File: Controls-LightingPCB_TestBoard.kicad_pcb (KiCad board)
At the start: 2 copper layers, 92 x 84 mm, 52 parts, among them J1 +12V, J10 REGEN SW, J11 CRUZ ST IND, J12 CRUZ EN IND, J13 REGEN IND, J14 NEU IND, J15 FOR IND, J16 REV IND, J17 EXT RBLINK, J18 EXT LBLINK, J19 INT RBLINK, J2 GND, J20 INT LBLINK, J21 EXT HDLT, J22 EXT BRAKE, J3 POWER MINION, J4 POWER LEADER, J5 TURN SIG SW, J6 CRUISE EN, J7 CRUISE SET, J8 HZD SW, J9 F/R SW, SW2 SW_SPST, SW3 SW_SPST, SW4 SW_SPST, SW6 SW_SPST, U1 SP3T, U2 SP3T

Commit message: update QUAC
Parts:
- added H1: MountingHole, MountingHole:MountingHole_3mm, F.Cu at (103.5, 62.0)
- added H2: MountingHole, MountingHole:MountingHole_3mm, F.Cu at (187.6, 62.2)
- added H3: MountingHole, MountingHole:MountingHole_3mm, F.Cu at (103.6, 142.2)
- added H4: MountingHole, MountingHole:MountingHole_3mm, F.Cu at (187.6, 142.2)
- added LOGO1: Logo_Placeholder, UTSVT_Special:UTSVT_Logo_Symbol, F.Cu at (174.6, 119.2)
- added LOGO2: Logo_Placeholder, UTSVT_Special:Hallock_Image_Tiny, B.Cu at (134.6, 66.2)
- J10, J15: footprint Connector_Molex:Molex_Micro-Fit_3.0_43650-0200_1x02_P3.00mm_Horizontal -> Connector_Molex:Molex_Micro-Fit_3.0_43650-0215_1x02_P3.00mm_Vertical
- moved D11 54.7 mm to (134.7, 84.3)
- moved D12 54.7 mm to (134.7, 97.0)
- moved D7 54.7 mm to (134.7, 122.4)
- moved D8 54.7 mm to (134.7, 109.7)
- moved J1 54.7 mm to (125.3, 68.6)
- moved J9 54.7 mm to (186.7, 75.6)
- moved R11 54.7 mm to (134.7, 80.0)
- moved R12 54.7 mm to (134.8, 92.2)
- moved R4 54.7 mm to (152.2, 105.0)
- moved R5 54.7 mm to (152.2, 92.2)
- moved R6 54.7 mm to (152.2, 116.9)
- moved R7 54.7 mm to (134.8, 116.9)
- moved R8 54.7 mm to (134.8, 105.0)
- moved SW2 54.7 mm to (164.3, 117.7)
- moved SW3 54.7 mm to (164.3, 104.5)
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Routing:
- net Net-(J1-Pad1): track 80.8 -> 64.4 mm
- net Net-(J2-Pad1): track 41.0 -> 29.9 mm
- net Net-(J10-Pad1): track 22.7 -> 24.6 mm
- net Net-(D5-Pad1): track 70.2 -> 71.4 mm
- net Net-(J15-Pad1): track 84.8 -> 85.3 mm
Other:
- board size 92 x 84 mm -> 92 x 88 mm
- board text added: "VER 0.1"

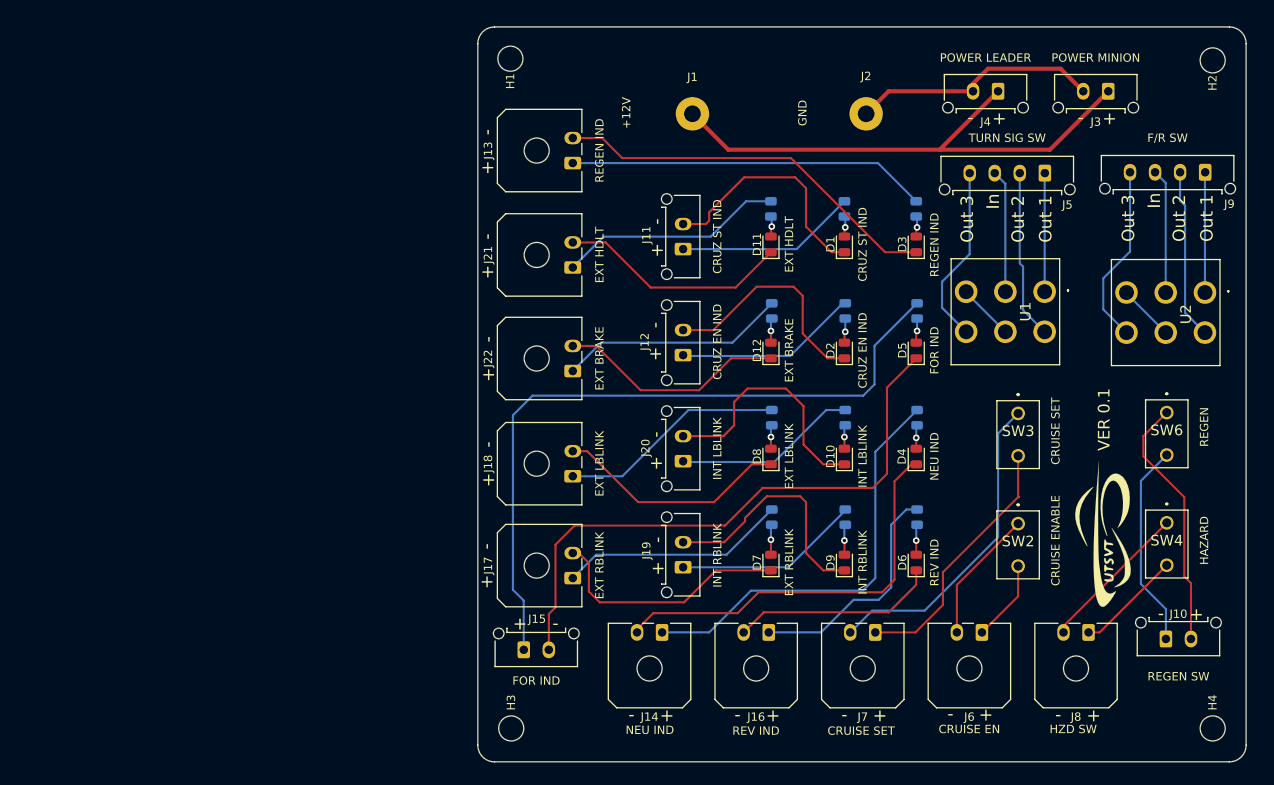
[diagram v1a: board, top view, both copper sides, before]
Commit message: checklist wrap up, and ground plane added
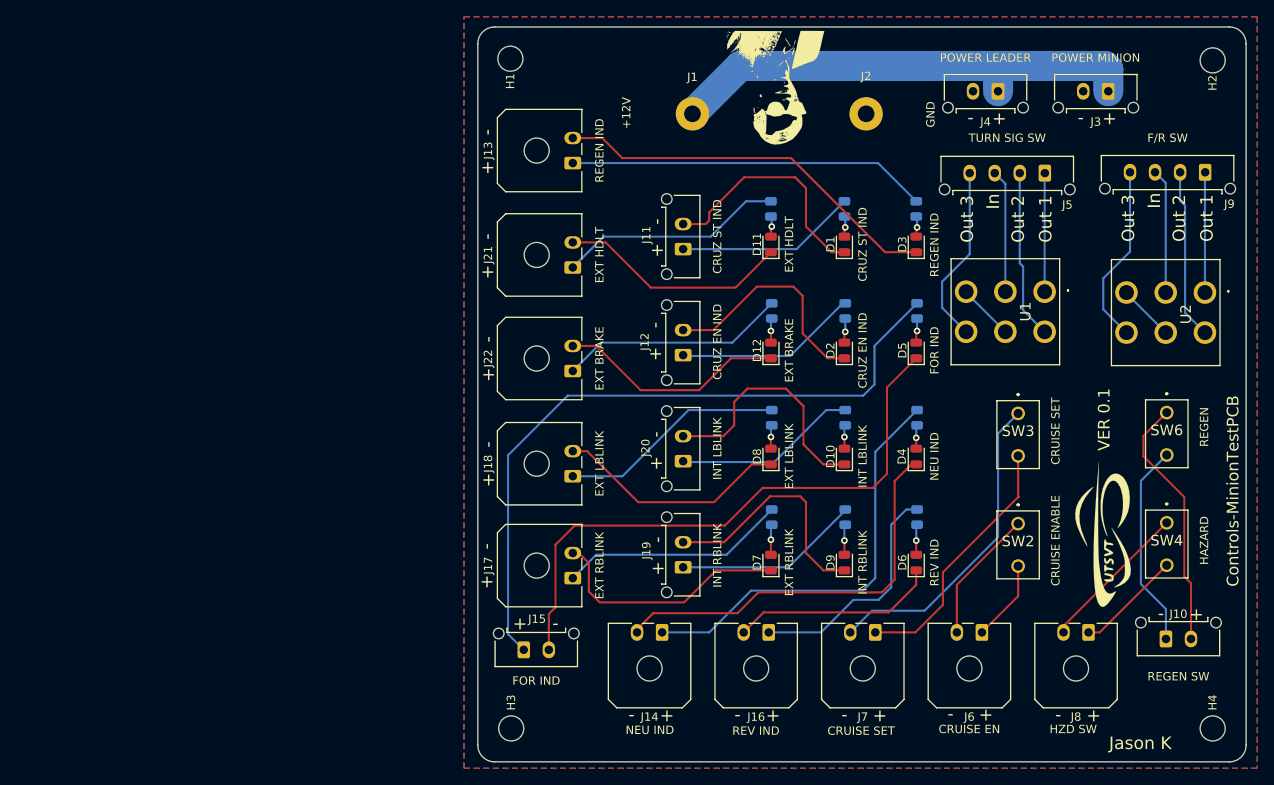
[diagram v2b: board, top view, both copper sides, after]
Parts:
- LOGO2: moved to F.Cu
- moved LOGO2 1.26 mm to (135.7, 65.7), turned to 180 degrees
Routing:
- net Net-(J2-Pad1): track 29.9 -> 0.00 mm
- net Net-(J1-Pad1): track 64.4 -> 58.0 mm
- net Net-(J15-Pad1): track 85.3 -> 83.3 mm
- added copper zone on B.Cu, net Net-(J2-Pad1)
- added copper zone on F.Cu, net Net-(J2-Pad1)
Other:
- board text added: "Controls-MinionTestPCB"
- board text added: "Jason K"

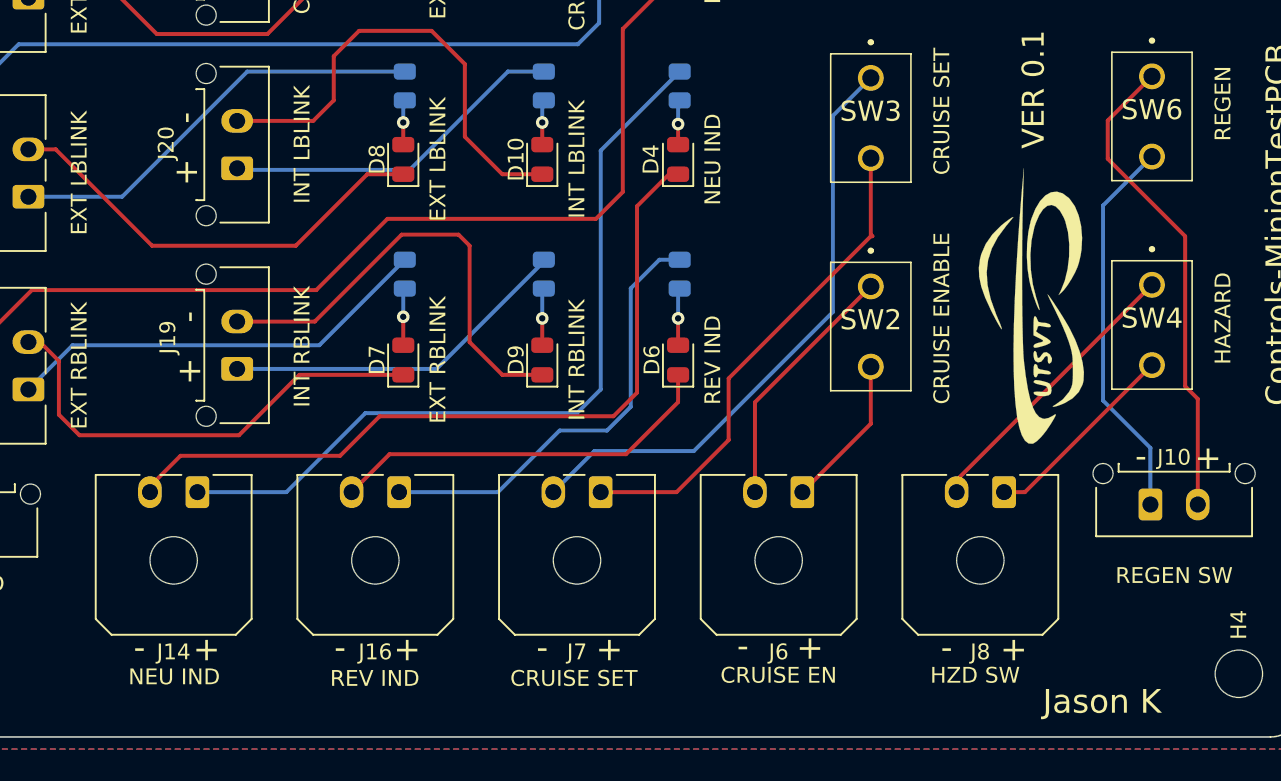
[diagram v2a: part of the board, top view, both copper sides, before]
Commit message: moved connectors to edge of board
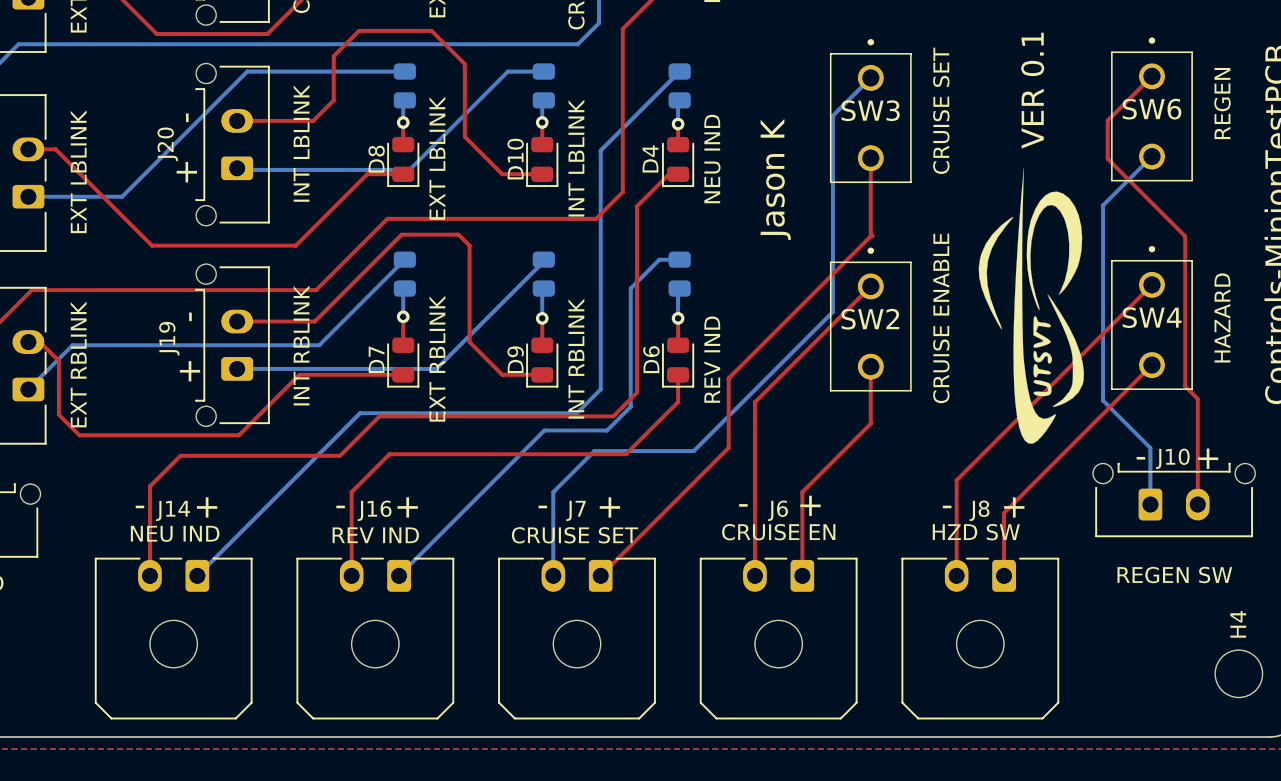
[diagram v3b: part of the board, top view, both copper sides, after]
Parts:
- moved J14 5.30 mm to (121.6, 136.0)
- moved J16 5.30 mm to (134.4, 136.0)
- moved J6 5.30 mm to (159.9, 136.0)
- moved J7 5.30 mm to (147.2, 136.0)
- moved J8 5.30 mm to (172.7, 136.0)
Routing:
- net Net-(J8-Pad2): track 18.2 -> 23.5 mm
- net Net-(J7-Pad2): track 38.2 -> 43.5 mm
- net Net-(J6-Pad2): track 16.1 -> 21.4 mm
- net Net-(J6-Pad1): track 9.74 -> 15.0 mm
- net Net-(D6-Pad1): track 24.8 -> 30.1 mm
- net Net-(D4-Pad1): track 48.9 -> 54.2 mm
- net Net-(J8-Pad1): track 12.7 -> 17.2 mm
- net Net-(J7-Pad1): track 31.2 -> 33.7 mm
- net Net-(J14-Pad1): track 50.4 -> 52.6 mm
- net Net-(J16-Pad1): track 28.3 -> 30.4 mm

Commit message: update spacing
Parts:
- moved D11 1.37 mm to (134.7, 85.6)
- moved D1 1.37 mm to (143.5, 85.6)
- moved D3 1.37 mm to (152.1, 85.6)
- moved D12 0.97 mm to (134.7, 97.9)
- moved D2 0.97 mm to (143.5, 97.9)
- moved D5 0.97 mm to (152.1, 97.9)
- moved D8 0.67 mm to (134.7, 110.3)
- moved D10 0.67 mm to (143.5, 110.3)
- moved D4 0.67 mm to (152.1, 110.3)
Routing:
- net Net-(D1-Pad1): track 28.6 -> 21.3 mm
- net Net-(D2-Pad1): track 27.7 -> 29.1 mm
- net Net-(D1-Pad2): track 2.48 -> 3.80 mm
- net Net-(D3-Pad2): track 2.48 -> 3.80 mm
- net Net-(D11-Pad2): track 2.48 -> 3.78 mm
- net Net-(D12-Pad2): track 2.93 -> 4.04 mm
- net Net-(D4-Pad1): track 54.2 -> 53.2 mm
- net Net-(D5-Pad2): track 2.93 -> 3.90 mm
- net Net-(D2-Pad2): track 2.93 -> 3.90 mm
- net Net-(D4-Pad2): track 2.84 -> 3.65 mm
- net Net-(D10-Pad2): track 2.84 -> 3.65 mm
- net Net-(D8-Pad2): track 2.84 -> 3.64 mm
- net Net-(D3-Pad1): track 46.8 -> 47.4 mm
- net Net-(D11-Pad1): track 27.7 -> 27.2 mm
